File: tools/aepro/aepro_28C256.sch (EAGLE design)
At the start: 22 parts, among them IC1 MCP23017SP, IC2 MCP23008/P, U1 328P, Y1 16 MHz

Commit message: Update several tool boards.
+ AEPRO had the wrong socket size; the ZIF footprint was for
  a narrow 28-pin DIP.
+ AEPRO was missing an inverter on the LEDs.
+ M328PGM had a serial line tied to RST: any attempt at using the
  UART caused the board to reset.
+ M1284PGM had no silkscreen markings to identify the board.
+ M1284PGM had no decoupling capacitor for the MCU.
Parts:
- added V1: 7404N, 74ttl-din:7404N
- R1, R2: value 4.7K -> (none)
- U$1: value AT28C256 -> AT28C256DIL28; device wntrmute:AT28C256 -> wntrmute:AT28C256DIL28
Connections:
- new net N$11: R5.1, V1/2.A
- new net N$15: R6.1, V1/1.A
- new net N$5: R4.1, V1/3.A
- net GND: now also V1/-UB.-UB, V1/4.A, V1/5.A, V1/6.A
- net N$2: now also V1/3.Y; no longer R4.1
- net N$3: now also V1/2.Y; no longer R5.1
- net N$4: now also V1/1.Y; no longer R6.1
- net VCC: now also V1/+UB.+UB
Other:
- moved on the sheet: D2, D3, D4, R4, R5, R6

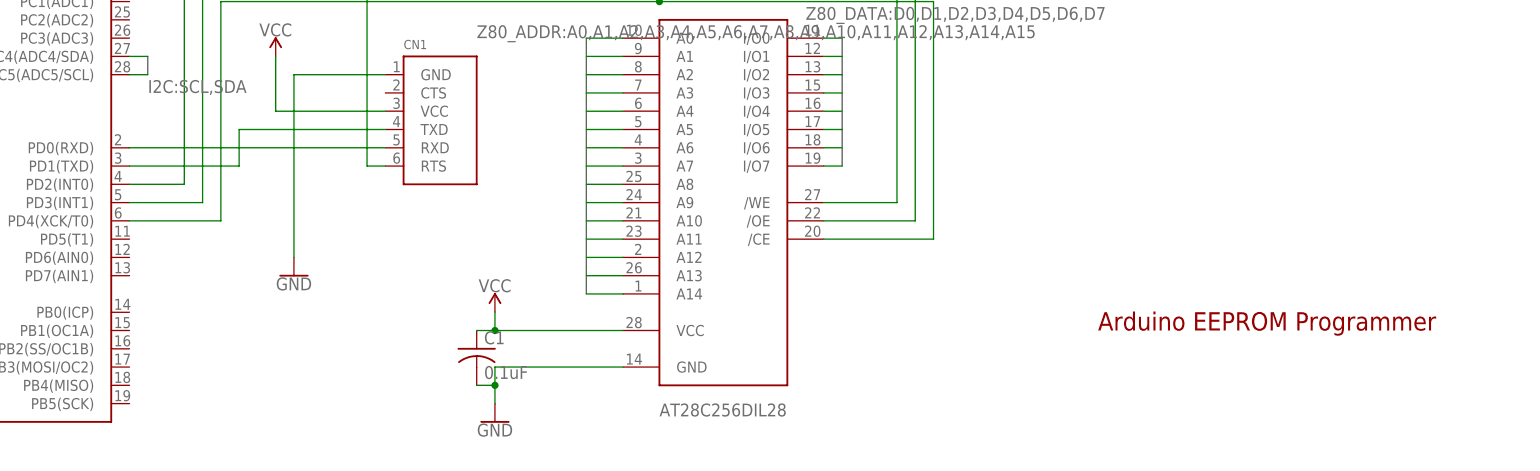
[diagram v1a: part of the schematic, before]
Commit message: Fix UART lines on AEPRO.
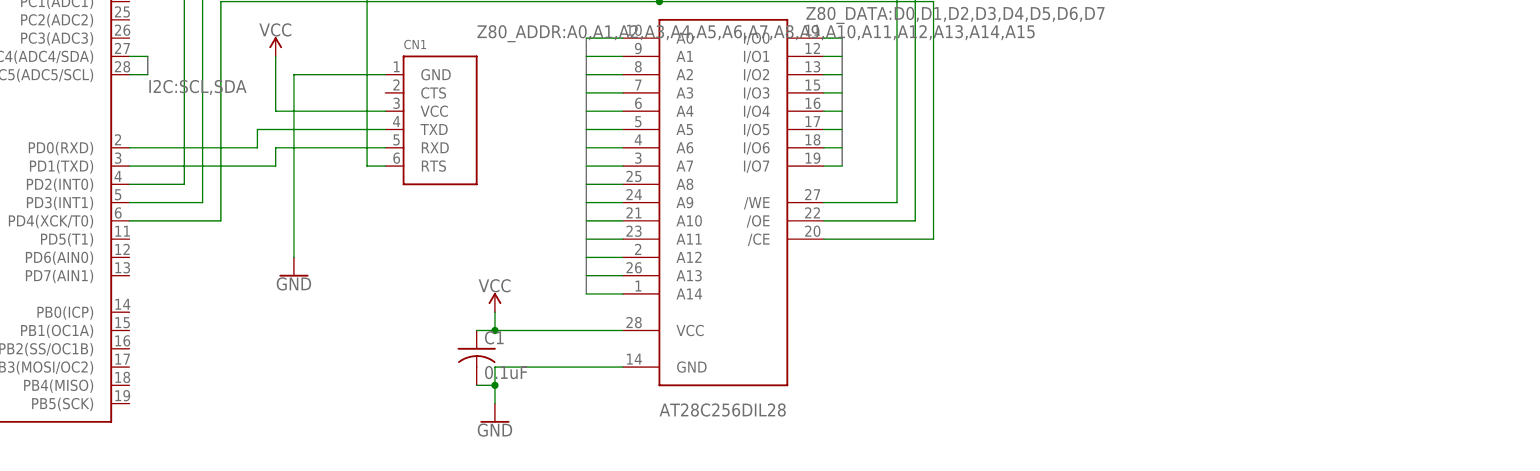
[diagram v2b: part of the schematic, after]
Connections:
- net N$12: now also CN1.TXD; no longer CN1.RXD
- net N$6: now also CN1.RXD; no longer CN1.TXD
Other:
- note removed: "Arduino EEPROM Programmer"
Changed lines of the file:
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@@
 <sheet>
 <plain>
-<text x="137.16" y="-15.24" size="2.54" layer="94">Arduino EEPROM Programmer</text>
 </plain>
 <instances>
@@
 <segment>
 <pinref part="U1" gate="U1" pin="PD1(TXD)"/>
-<wire x1="17.78" y1="7.62" x2="2.54" y2="7.62" width="0.1524" layer="91"/>
-<wire x1="17.78" y1="7.62" x2="17.78" y2="12.7" width="0.1524" layer="91"/>
-<pinref part="CN1" gate="G$1" pin="TXD"/>
-<wire x1="17.78" y1="12.7" x2="38.1" y2="12.7" width="0.1524" layer="91"/>
+<wire x1="22.86" y1="7.62" x2="2.54" y2="7.62" width="0.1524" layer="91"/>
+<wire x1="22.86" y1="7.62" x2="22.86" y2="10.16" width="0.1524" layer="91"/>
+<pinref part="CN1" gate="G$1" pin="RXD"/>
+<wire x1="22.86" y1="10.16" x2="38.1" y2="10.16" width="0.1524" layer="91"/>
 </segment>
 </net>
@@
 </segment>
 </net>
-<net name="N$12" class="0">
-<segment>
-<pinref part="CN1" gate="G$1" pin="RXD"/>
-<pinref part="U1" gate="U1" pin="PD0(RXD)"/>
-<wire x1="38.1" y1="10.16" x2="2.54" y2="10.16" width="0.1524" layer="91"/>
-</segment>
-</net>
 <net name="N$13" class="0">
 <segment>
@@
 </segment>
 </net>
+<net name="N$12" class="0">
+<segment>
+<pinref part="CN1" gate="G$1" pin="TXD"/>
+<wire x1="38.1" y1="12.7" x2="20.32" y2="12.7" width="0.1524" layer="91"/>
+<wire x1="20.32" y1="12.7" x2="20.32" y2="10.16" width="0.1524" layer="91"/>
+<pinref part="U1" gate="U1" pin="PD0(RXD)"/>
+<wire x1="20.32" y1="10.16" x2="2.54" y2="10.16" width="0.1524" layer="91"/>
+</segment>
+</net>

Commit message: AEPRO rev 7
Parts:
- U$1: value AT28C256DIL28 -> AT28C256; device wntrmute:AT28C256DIL28 -> wntrmute:AT28C256
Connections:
- net N$2 renamed WE
- net N$3 renamed OE
- net N$4 renamed CE
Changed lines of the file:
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@@
 </classes>
 <parts>
-<part name="U$1" library="wntrmute" deviceset="AT28C256" device="DIL28" value="AT28C256DIL28"/>
+<part name="U$1" library="wntrmute" deviceset="AT28C256" device="" value="AT28C256"/>
 <part name="SUPPLY1" library="SparkFun-PowerSymbols" deviceset="VCC" device=""/>
 <part name="SUPPLY2" library="SparkFun-PowerSymbols" deviceset="VCC" device=""/>
@@
 </segment>
 </net>
-<net name="N$2" class="0">
+<net name="WE" class="0">
 <segment>
 <pinref part="V1" gate="/3" pin="Y"/>
@@
 </segment>
 </net>
-<net name="N$3" class="0">
+<net name="OE" class="0">
 <segment>
 <pinref part="V1" gate="/2" pin="Y"/>
@@
 </segment>
 </net>
-<net name="N$4" class="0">
+<net name="CE" class="0">
 <segment>
 <pinref part="V1" gate="/1" pin="Y"/>
